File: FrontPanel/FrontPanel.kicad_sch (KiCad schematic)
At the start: 26 parts, among them SW11 Decimal, SW12 0, SW13 Backspace, SW14 Current 2, SW15 Cancel, SW21 1, SW22 2, SW23 3, SW24 Voltage 2, SW25 Confirm, SW31 4, SW32 5, SW33 6, SW34 Current 1, SW35 Channel 2, SW41 7, SW42 8, SW43 9, SW44 Voltage 1, SW45 Channel 1

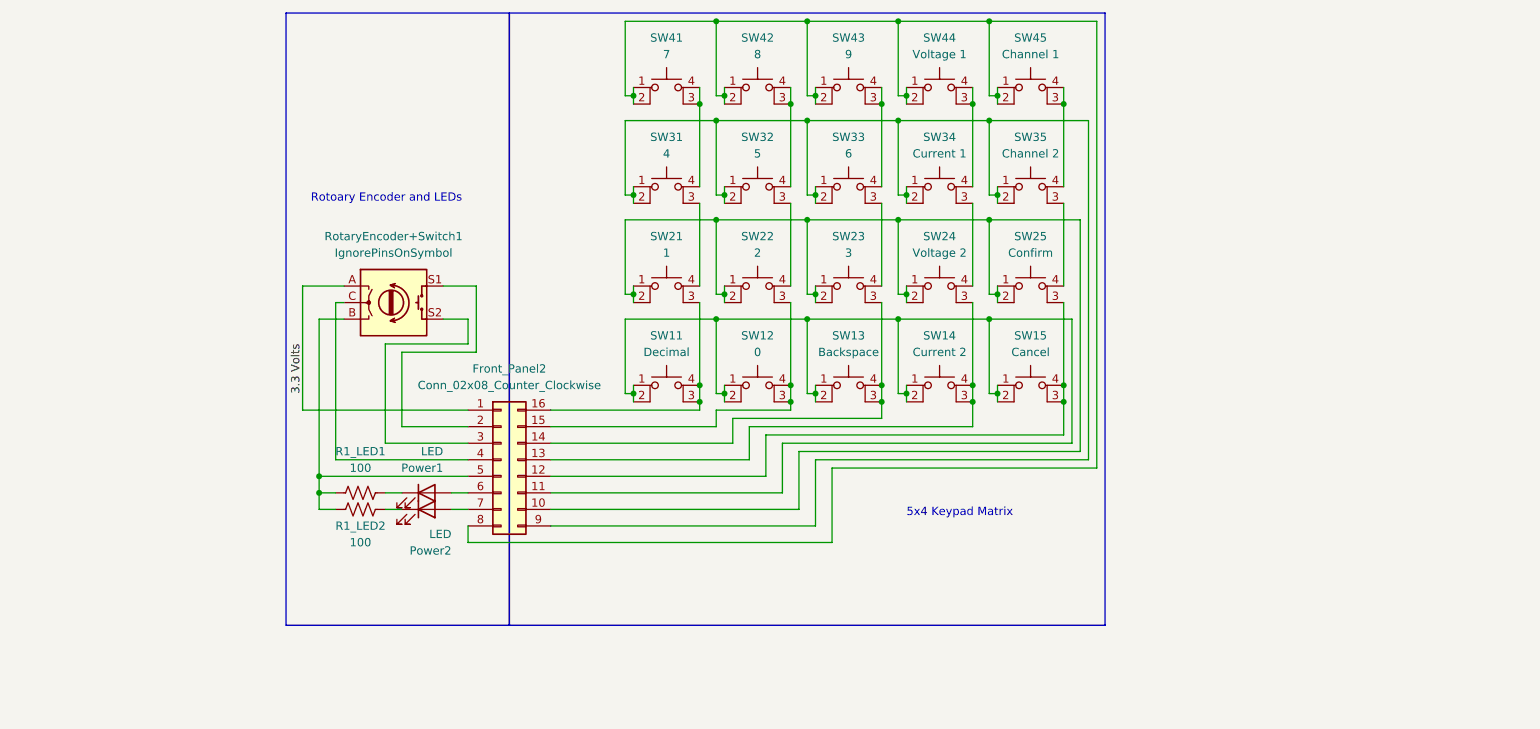
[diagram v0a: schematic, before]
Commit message: Fixed button footprints
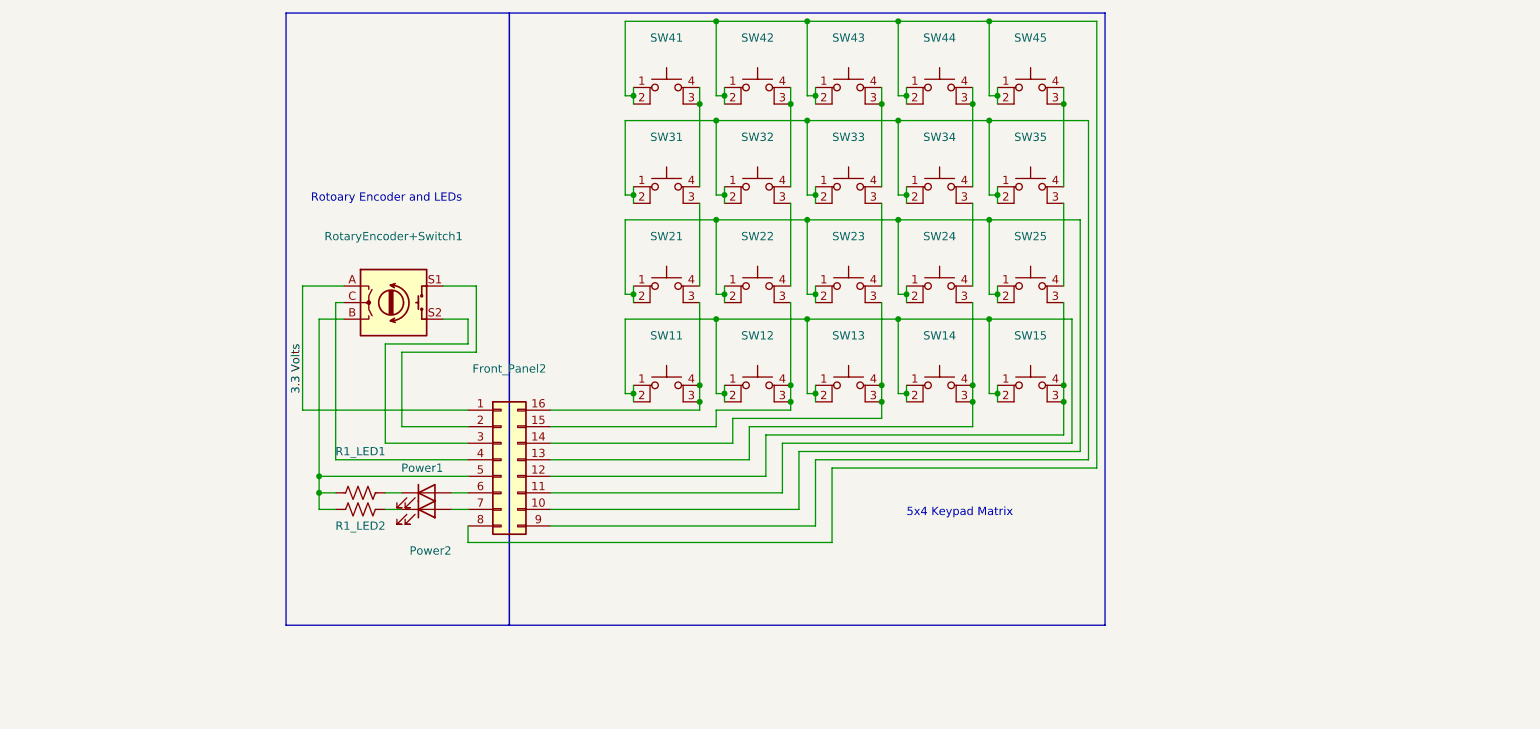
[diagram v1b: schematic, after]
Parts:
- Front_Panel2: value Conn_02x08_Counter_Clockwise -> (none); footprint Connector_IDC:IDC-Header_2x08_P2.54mm_Vertical -> (none)
- Power1, Power2: value LED -> (none); footprint LED_THT:LED_D3.0mm -> (none)
- R1_LED1, R1_LED2: value 100 -> (none); footprint Resistor_SMD:R_0603_1608Metric -> (none)
- RotaryEncoder+Switch1: value IgnorePinsOnSymbol -> (none); footprint Rotary_Encoder:RotaryEncoder_Alps_EC11E-Switch_Vertical_H20mm -> (none)
- SW11: value Decimal -> (none); footprint Button_Switch_SMD:SW_MEC_5GSH9 -> (none)
- SW12: value 0 -> (none); footprint Button_Switch_SMD:SW_MEC_5GSH9 -> (none)
- SW13: value Backspace -> (none); footprint Button_Switch_SMD:SW_MEC_5GSH9 -> (none)
- SW14: value Current 2 -> (none); footprint Button_Switch_SMD:SW_MEC_5GSH9 -> (none)
- SW15: value Cancel -> (none); footprint Button_Switch_SMD:SW_MEC_5GSH9 -> (none)
- SW21: value 1 -> (none); footprint Button_Switch_SMD:SW_MEC_5GSH9 -> (none)
- SW22: value 2 -> (none); footprint Button_Switch_SMD:SW_MEC_5GSH9 -> (none)
- SW23: value 3 -> (none); footprint Button_Switch_SMD:SW_MEC_5GSH9 -> (none)
- SW24: value Voltage 2 -> (none); footprint Button_Switch_SMD:SW_MEC_5GSH9 -> (none)
- SW25: value Confirm -> (none); footprint Button_Switch_SMD:SW_MEC_5GSH9 -> (none)
- SW31: value 4 -> (none); footprint Button_Switch_SMD:SW_MEC_5GSH9 -> (none)
- SW32: value 5 -> (none); footprint Button_Switch_SMD:SW_MEC_5GSH9 -> (none)
- SW33: value 6 -> (none); footprint Button_Switch_SMD:SW_MEC_5GSH9 -> (none)
- SW34: value Current 1 -> (none); footprint Button_Switch_SMD:SW_MEC_5GSH9 -> (none)
- SW35: value Channel 2 -> (none); footprint Button_Switch_SMD:SW_MEC_5GSH9 -> (none)
- SW41: value 7 -> (none); footprint Button_Switch_SMD:SW_MEC_5GSH9 -> (none)
- SW42: value 8 -> (none); footprint Button_Switch_SMD:SW_MEC_5GSH9 -> (none)
- SW43: value 9 -> (none); footprint Button_Switch_SMD:SW_MEC_5GSH9 -> (none)
- SW44: value Voltage 1 -> (none); footprint Button_Switch_SMD:SW_MEC_5GSH9 -> (none)
- SW45: value Channel 1 -> (none); footprint Button_Switch_SMD:SW_MEC_5GSH9 -> (none)

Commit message: Grouped up keypad
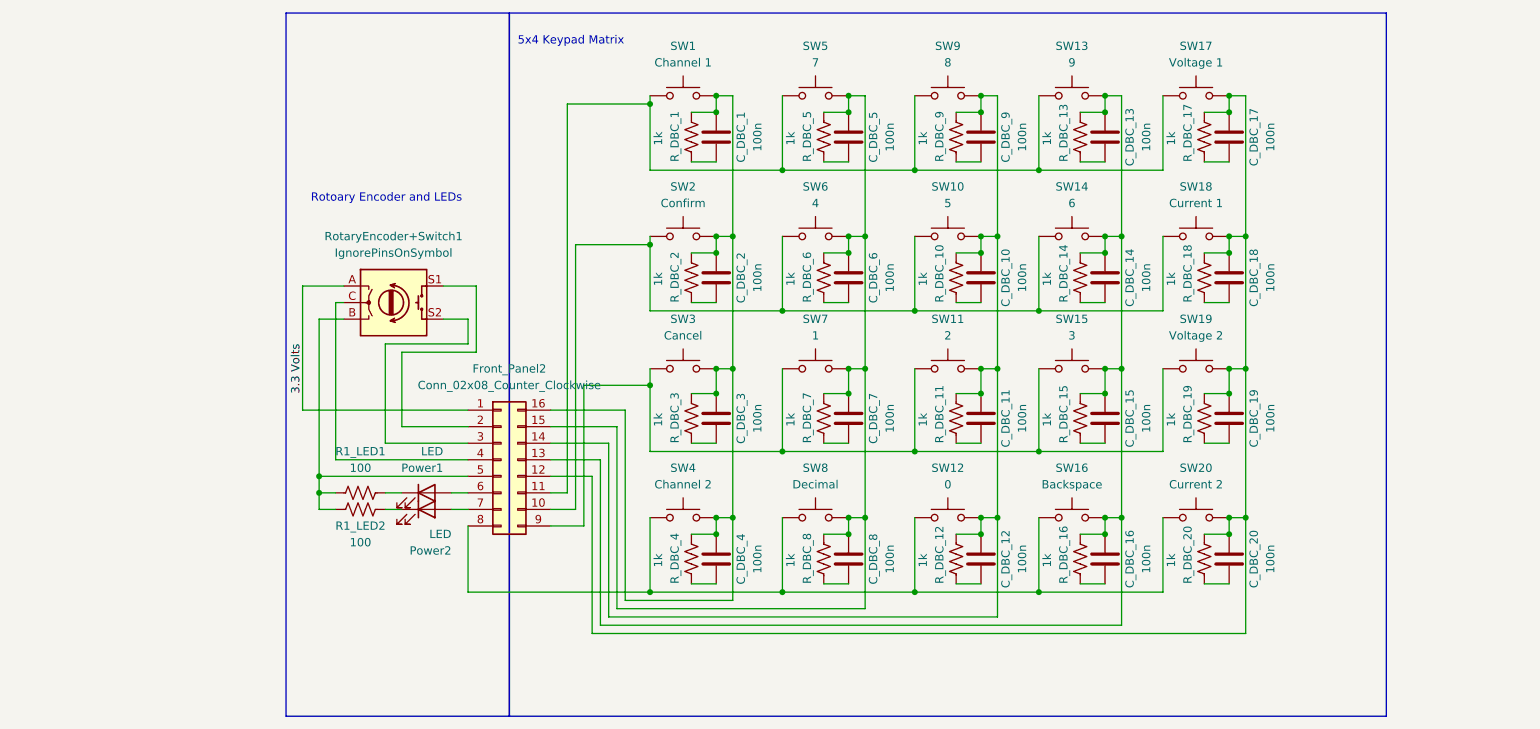
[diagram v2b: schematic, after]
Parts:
- added C_DBC_1, C_DBC_10, C_DBC_11, C_DBC_12, C_DBC_13, C_DBC_14, C_DBC_15, C_DBC_16, C_DBC_17, C_DBC_18, C_DBC_19, C_DBC_2, C_DBC_20, C_DBC_3, C_DBC_4, C_DBC_5, C_DBC_6, C_DBC_7, C_DBC_8, C_DBC_9: 100n, Capacitor_SMD:C_0603_1608Metric, symbol Device:C
- added R_DBC_1, R_DBC_10, R_DBC_11, R_DBC_12, R_DBC_13, R_DBC_14, R_DBC_15, R_DBC_16, R_DBC_17, R_DBC_18, R_DBC_19, R_DBC_2, R_DBC_20, R_DBC_3, R_DBC_4, R_DBC_5, R_DBC_6, R_DBC_7, R_DBC_8, R_DBC_9: 1k, Resistor_SMD:R_0603_1608Metric, symbol Device:R_US
- Front_Panel2: value (none) -> Conn_02x08_Counter_Clockwise; footprint (none) -> Connector_IDC:IDC-Header_2x08_P2.54mm_Vertical
- Power1, Power2: value (none) -> LED; footprint (none) -> LED_THT:LED_D3.0mm
- R1_LED1, R1_LED2: value (none) -> 100; footprint (none) -> Resistor_SMD:R_0603_1608Metric
- RotaryEncoder+Switch1: value (none) -> IgnorePinsOnSymbol; footprint (none) -> Rotary_Encoder:RotaryEncoder_Alps_EC11E-Switch_Vertical_H20mm
- SW1: renamed from SW45; value (none) -> Channel 1; footprint (none) -> Button_Switch_THT:SW_PUSH-12mm; symbol Switch:SW_MEC_5E -> Switch:SW_Push
- SW10: renamed from SW32; value (none) -> 5; footprint (none) -> Button_Switch_THT:SW_PUSH-12mm; symbol Switch:SW_MEC_5E -> Switch:SW_Push
- SW11: renamed from SW22; value (none) -> 2; footprint (none) -> Button_Switch_THT:SW_PUSH-12mm; symbol Switch:SW_MEC_5E -> Switch:SW_Push
- SW12: value (none) -> 0; footprint (none) -> Button_Switch_THT:SW_PUSH-12mm; symbol Switch:SW_MEC_5E -> Switch:SW_Push
- SW13: renamed from SW43; value (none) -> 9; footprint (none) -> Button_Switch_THT:SW_PUSH-12mm; symbol Switch:SW_MEC_5E -> Switch:SW_Push
- SW14: renamed from SW33; value (none) -> 6; footprint (none) -> Button_Switch_THT:SW_PUSH-12mm; symbol Switch:SW_MEC_5E -> Switch:SW_Push
- SW15: renamed from SW23; value (none) -> 3; footprint (none) -> Button_Switch_THT:SW_PUSH-12mm; symbol Switch:SW_MEC_5E -> Switch:SW_Push
- SW16: renamed from SW13; value (none) -> Backspace; footprint (none) -> Button_Switch_THT:SW_PUSH-12mm; symbol Switch:SW_MEC_5E -> Switch:SW_Push
- SW17: renamed from SW44; value (none) -> Voltage 1; footprint (none) -> Button_Switch_THT:SW_PUSH-12mm; symbol Switch:SW_MEC_5E -> Switch:SW_Push
- SW18: renamed from SW34; value (none) -> Current 1; footprint (none) -> Button_Switch_THT:SW_PUSH-12mm; symbol Switch:SW_MEC_5E -> Switch:SW_Push
- SW19: renamed from SW24; value (none) -> Voltage 2; footprint (none) -> Button_Switch_THT:SW_PUSH-12mm; symbol Switch:SW_MEC_5E -> Switch:SW_Push
- SW2: renamed from SW25; value (none) -> Confirm; footprint (none) -> Button_Switch_THT:SW_PUSH-12mm; symbol Switch:SW_MEC_5E -> Switch:SW_Push
- SW20: renamed from SW14; value (none) -> Current 2; footprint (none) -> Button_Switch_THT:SW_PUSH-12mm; symbol Switch:SW_MEC_5E -> Switch:SW_Push
- SW3: renamed from SW15; value (none) -> Cancel; footprint (none) -> Button_Switch_THT:SW_PUSH-12mm; symbol Switch:SW_MEC_5E -> Switch:SW_Push
- SW4: renamed from SW35; value (none) -> Channel 2; footprint (none) -> Button_Switch_THT:SW_PUSH-12mm; symbol Switch:SW_MEC_5E -> Switch:SW_Push
- SW5: renamed from SW41; value (none) -> 7; footprint (none) -> Button_Switch_THT:SW_PUSH-12mm; symbol Switch:SW_MEC_5E -> Switch:SW_Push
- SW6: renamed from SW31; value (none) -> 4; footprint (none) -> Button_Switch_THT:SW_PUSH-12mm; symbol Switch:SW_MEC_5E -> Switch:SW_Push
- SW7: renamed from SW21; value (none) -> 1; footprint (none) -> Button_Switch_THT:SW_PUSH-12mm; symbol Switch:SW_MEC_5E -> Switch:SW_Push
- SW8: renamed from SW11; value (none) -> Decimal; footprint (none) -> Button_Switch_THT:SW_PUSH-12mm; symbol Switch:SW_MEC_5E -> Switch:SW_Push
- SW9: renamed from SW42; value (none) -> 8; footprint (none) -> Button_Switch_THT:SW_PUSH-12mm; symbol Switch:SW_MEC_5E -> Switch:SW_Push
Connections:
- new net: C_DBC_19.1, R_DBC_19.2
- new net: C_DBC_17.2, C_DBC_18.2, C_DBC_19.2, C_DBC_20.2, Front_Panel2.12 (Pin_12), R_DBC_17.1, R_DBC_18.1, R_DBC_19.1, R_DBC_20.1, SW17.2, SW18.2, SW19.2, SW20.2
- new net: Front_Panel2.10 (Pin_10), SW10.1, SW14.1, SW18.1, SW2.1, SW6.1
- new net: C_DBC_13.2, C_DBC_14.2, C_DBC_15.2, C_DBC_16.2, Front_Panel2.13 (Pin_13), R_DBC_13.1, R_DBC_14.1, R_DBC_15.1, R_DBC_16.1, SW13.2, SW14.2, SW15.2, SW16.2
- new net: C_DBC_20.1, R_DBC_20.2
- new net: C_DBC_18.1, R_DBC_18.2
- new net: Front_Panel2.8 (Pin_8), SW12.1, SW16.1, SW20.1, SW4.1, SW8.1
- new net: C_DBC_10.2, C_DBC_11.2, C_DBC_12.2, C_DBC_9.2, Front_Panel2.14 (Pin_14), R_DBC_10.1, R_DBC_11.1, R_DBC_12.1, R_DBC_9.1, SW10.2, SW11.2, SW12.2, SW9.2
- new net: Front_Panel2.9 (Pin_9), SW11.1, SW15.1, SW19.1, SW3.1, SW7.1
- new net: C_DBC_8.1, R_DBC_8.2
- new net: C_DBC_5.2, C_DBC_6.2, C_DBC_7.2, C_DBC_8.2, Front_Panel2.15 (Pin_15), R_DBC_5.1, R_DBC_6.1, R_DBC_7.1, R_DBC_8.1, SW5.2, SW6.2, SW7.2, SW8.2
- new net: C_DBC_1.2, C_DBC_2.2, C_DBC_3.2, C_DBC_4.2, Front_Panel2.16 (Pin_16), R_DBC_1.1, R_DBC_2.1, R_DBC_3.1, R_DBC_4.1, SW1.2, SW2.2, SW3.2, SW4.2
- new net: C_DBC_2.1, R_DBC_2.2
- new net: C_DBC_1.1, R_DBC_1.2
- new net: C_DBC_3.1, R_DBC_3.2
- new net: C_DBC_13.1, R_DBC_13.2
- new net: C_DBC_12.1, R_DBC_12.2
- new net: C_DBC_17.1, R_DBC_17.2
- new net: C_DBC_5.1, R_DBC_5.2
- new net: Front_Panel2.11 (Pin_11), SW1.1, SW13.1, SW17.1, SW5.1, SW9.1
- new net: C_DBC_15.1, R_DBC_15.2
- new net: C_DBC_14.1, R_DBC_14.2
- new net: C_DBC_11.1, R_DBC_11.2
- new net: C_DBC_6.1, R_DBC_6.2
- new net: C_DBC_9.1, R_DBC_9.2
- new net: C_DBC_10.1, R_DBC_10.2
- new net: C_DBC_4.1, R_DBC_4.2
- new net: C_DBC_7.1, R_DBC_7.2
- new net: C_DBC_16.1, R_DBC_16.2

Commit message: Front Panel
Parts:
- added C_DBC_21, C_DBC_22, C_DBC_23: 100n, Capacitor_SMD:C_0603_1608Metric, symbol Device:C
- added R_DBC_21, R_DBC_22, R_DBC_23: 1k, Resistor_SMD:R_0603_1608Metric, symbol Device:R_US
- Power1: renamed from Power2; footprint LED_THT:LED_D3.0mm -> LED_SMD:LED_0603_1608Metric
- Power2: renamed from Power1; footprint LED_THT:LED_D3.0mm -> LED_SMD:LED_0603_1608Metric
- renumbered R1_LED2 to R1, R1_LED1 to R2
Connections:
- net at C_DBC_17.2, C_DBC_18.2, C_DBC_19.2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: now also Front_Panel2.11 (Pin_11); no longer Front_Panel2.12 (Pin_12)
- net at SW10.1, SW14.1, SW18.1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: now also Front_Panel2.14 (Pin_14); no longer Front_Panel2.10 (Pin_10)
- net at C_DBC_13.2, C_DBC_14.2, C_DBC_15.2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: now also Front_Panel2.10 (Pin_10); no longer Front_Panel2.13 (Pin_13)
- net at SW12.1, SW16.1, SW20.1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: now also Front_Panel2.16 (Pin_16); no longer Front_Panel2.8 (Pin_8)
- net at C_DBC_10.2, C_DBC_11.2, C_DBC_12.2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: now also Front_Panel2.9 (Pin_9); no longer Front_Panel2.14 (Pin_14)
- net at SW11.1, SW15.1, SW19.1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: now also Front_Panel2.15 (Pin_15); no longer Front_Panel2.9 (Pin_9)
- net at C_DBC_5.2, C_DBC_6.2, C_DBC_7.2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: now also Front_Panel2.8 (Pin_8); no longer Front_Panel2.15 (Pin_15)
- net at C_DBC_1.2, C_DBC_2.2, C_DBC_3.2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: now also Front_Panel2.7 (Pin_7); no longer Front_Panel2.16 (Pin_16)
- net at Power1.2 (A): now also Front_Panel2.3 (Pin_3); no longer Front_Panel2.7 (Pin_7)
- net at R1.2, R2.2: now also Front_Panel2.1 (Pin_1), RotaryEncoder+Switch1.C, RotaryEncoder+Switch1.S2, C_DBC_21.1, C_DBC_22.2; no longer Front_Panel2.5 (Pin_5), RotaryEncoder+Switch1.B
- net at SW1.1, SW13.1, SW17.1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: now also Front_Panel2.13 (Pin_13); no longer Front_Panel2.11 (Pin_11)
- net at RotaryEncoder+Switch1.S1: now also Front_Panel2.6 (Pin_6), C_DBC_23.1, R_DBC_23.2; no longer Front_Panel2.2 (Pin_2)
- net at Front_Panel2.4 (Pin_4): now also R_DBC_21.1; no longer RotaryEncoder+Switch1.C
- net at Power2.2 (A): now also Front_Panel2.2 (Pin_2); no longer Front_Panel2.6 (Pin_6)
- net 3.3 Volts: no longer names the net of RotaryEncoder+Switch1.A
- net 3.3 Volts: now also C_DBC_22.1, R_DBC_22.1; no longer Front_Panel2.1 (Pin_1)
- new net: C_DBC_23.2, R_DBC_23.1
- new net: C_DBC_21.2, R_DBC_21.2, RotaryEncoder+Switch1.B
- new net: Front_Panel2.5 (Pin_5), R_DBC_22.2
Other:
- moved on the sheet: Power1, Power2, R1, R2, RotaryEncoder+Switch1
